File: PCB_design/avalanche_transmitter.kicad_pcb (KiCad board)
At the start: 2 copper layers, 55 x 110 mm, 31 parts, among them J1 Conn_01x07_Pin, Q1 2N3904, SW2 SW_SPDT, U1 74HC00

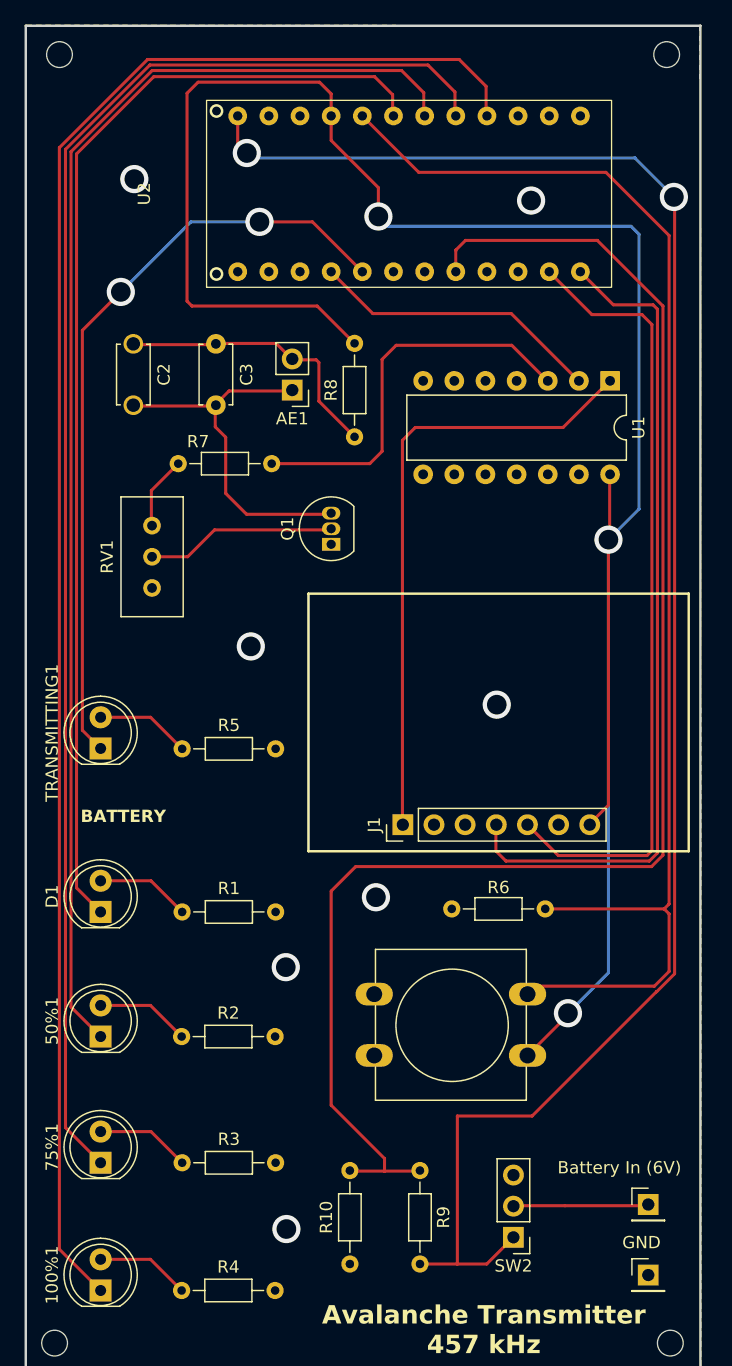
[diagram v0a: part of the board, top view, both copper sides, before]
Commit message: adjusted MCU footprint and hole diameter
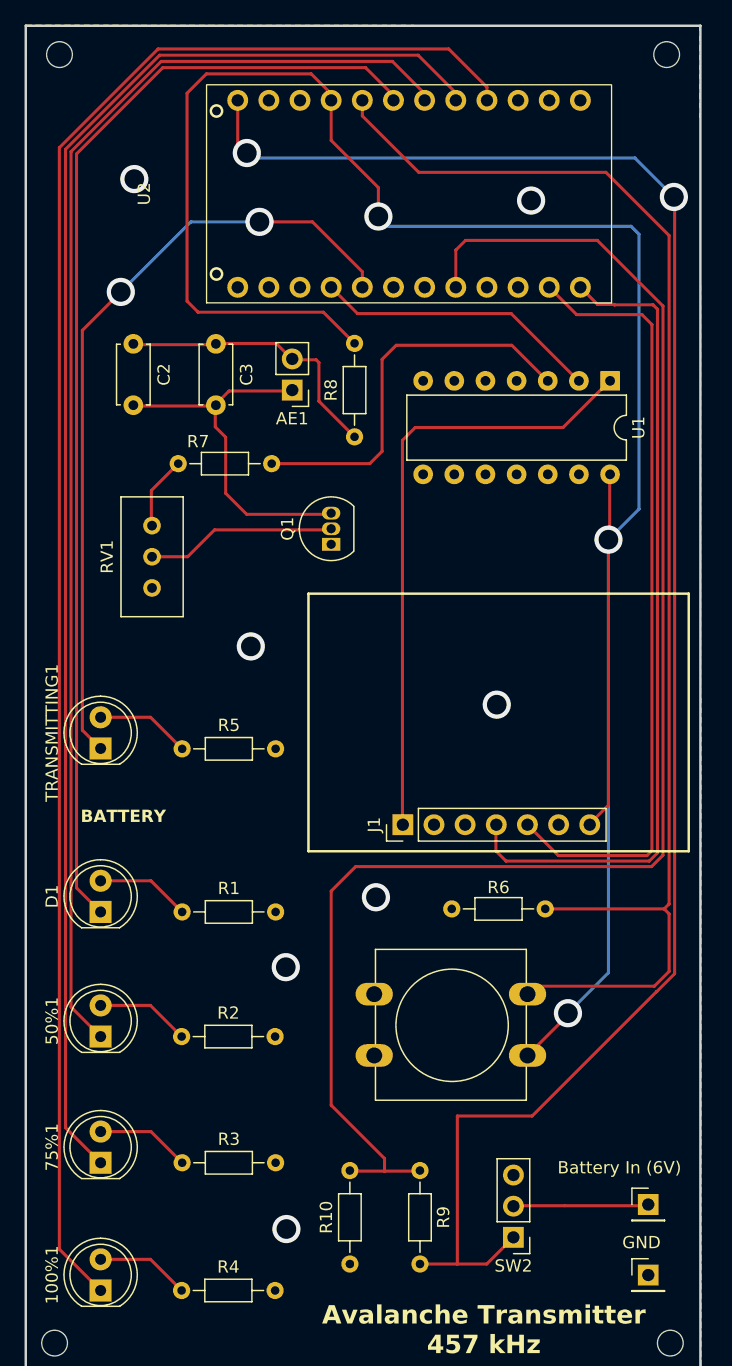
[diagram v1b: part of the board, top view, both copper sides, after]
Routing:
- net Net-(TRANSMITTING1-K): track 62.6 -> 64.0 mm
- net /on/off: track 146.1 -> 147.4 mm
- net Net-(U2-A1): track 124.6 -> 125.8 mm
- net Net-(U2-8): track 111.4 -> 112.7 mm
- net +3V0: track 177.9 -> 178.8 mm
- net Net-(J1-Pin_5): track 64.5 -> 63.9 mm
- net Net-(U2-12): track 23.9 -> 23.3 mm
- net Net-(D1-K): track 93.3 -> 92.7 mm
- net Net-(50%1-K): track 107.2 -> 106.7 mm
- net Net-(J1-Pin_4): track 67.9 -> 67.4 mm

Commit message: pcb finished
pcb finished. gerber files and source uploaded
receipt for oshpark print in folder
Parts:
- 75%: renamed from 50%1; value RED_LED_50 -> RED_LED
- AE1: value Antenna_Loop -> ANT_IN
- moved 100% 91.9 mm to (126.1, 114.5)
- moved 25% 91.9 mm to (126.1, 145.3)
- moved Battery In (6V) 91.9 mm to (170.8, 138.3)
- moved C1 91.9 mm to (135.5, 68.2)
- moved GND 91.9 mm to (170.8, 144.1)
- moved J1 91.9 mm to (150.8, 107.4)
- moved Q1 91.9 mm to (144.9, 84.5)
- moved R1 91.9 mm to (132.8, 114.5)
- moved R10 91.9 mm to (146.5, 143.2)
- moved R4 91.9 mm to (132.7, 145.3)
- moved R5 91.9 mm to (132.8, 101.2)
- moved R6 91.9 mm to (162.4, 114.2)
- moved R7 91.9 mm to (132.5, 77.9)
- moved R9 91.9 mm to (152.2, 135.5)
- moved REF** 91.9 mm to (172.6, 149.6)
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- renumbered D1 to 100%, 100%1 to 25%, 75%1 to 50%, C3 to C1, C2 to CV1, SW2 to On/Off, TRANSMITTING1 to TRANSMITTING
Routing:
- net +3V0: track 178.8 -> 182.4 mm
- net Net-(Q1-C): track 30.0 -> 29.5 mm
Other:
- board text added: "74HC00"
- board text added: "Battery Check"
- board text added: "GREEN_LED"
- board text added: "Mini Pro"
- board text added: "Power 6V"
- board text added: "RED_LED"
- board text added: "Si5351"
